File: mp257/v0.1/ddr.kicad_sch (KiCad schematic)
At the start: 61 parts, among them U1 STM32MP257FAK3, U15 MT40A1G16TB-062E IT:F

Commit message: Caps
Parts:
- added C158: 100nF_0402_16V, 4ms_Capacitor:C_0402, symbol 4ms_Capacitor:100nF_0402_16V
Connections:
- net GND: now also C158.2
- net VPP_DDR: now also C158.1
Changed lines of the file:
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@@
 	)
 	(junction
+		(at 208.28 243.84)
+		(diameter 0)
+		(color 0 0 0 0)
+	)
+	(junction
 		(at 241.3 123.19)
 		(diameter 0)
@@
 	(wire
 		(pts
+			(xy 198.12 251.46) (xy 208.28 251.46)
+		)
+		(stroke
+			(width 0)
+			(type default)
+		)
+	)
+	(wire
+		(pts
 			(xy 241.3 123.19) (xy 241.3 120.65)
 		)
@@
 	(wire
 		(pts
+			(xy 208.28 243.84) (xy 198.12 243.84)
+		)
+		(stroke
+			(width 0)
+			(type default)
+		)
+	)
+	(wire
+		(pts
 			(xy 241.3 135.89) (xy 241.3 143.51)
 		)
@@
 		)
 	)
+	(wire
+		(pts
+			(xy 198.12 243.84) (xy 198.12 246.38)
+		)
+		(stroke
+			(width 0)
+			(type default)
+		)
+	)
 	(label "DDR_A13"
 		(at 349.25 59.69 0)
@@
 					(unit 1)
 				)
+			)
+		)
+	)
+	(symbol
+		(lib_id "4ms_Capacitor:100nF_0402_16V")
+		(at 198.12 248.92 0)
+		(unit 1)
+		(exclude_from_sim no)
+		(in_bom yes)
+		(on_board yes)
+		(dnp no)
+		(fields_autoplaced yes)
+		(property "Reference" "C158"
+			(at 195.58 247.6562 0)
+			(effects
+				(font
+					(size 1.27 1.27)
+				)
+				(justify right)
+			)
+		)
+		(property "Value" "100nF_0402_16V"
+			(at 198.12 245.11 0)
+			(effects
+				(font
+					(size 1.27 1.27)
+				)
+				(hide yes)
+			)
+		)
+		(property "Footprint" "4ms_Capacitor:C_0402"
+			(at 195.58 254 0)
+			(effects
+				(font
+					(size 1.27 1.27)
+				)
+				(justify left)
+				(hide yes)
+			)
+		)
+		(property "Datasheet" ""
+			(at 198.12 248.92 0)
+			(effects
+				(font
+					(size 1.27 1.27)
+				)
+				(hide yes)
+			)
+		)
+		(property "Description" "0.1uF, Min. 16V 10%, X7R or X5R or similar"
+			(at 198.12 248.92 0)
+			(effects
+				(font
+					(size 1.27 1.27)
+				)
+				(hide yes)
+			)
+		)
+		(property "Specifications" "0.1uF, Min. 16V 10%, X7R or X5R or similar"
+			(at 195.58 256.794 0)
+			(effects
+				(font
+					(size 1.27 1.27)
+				)
+				(justify left)
+				(hide yes)
+			)
+		)
+		(property "Manufacturer" "Murata"
+			(at 195.58 258.318 0)
+			(effects
+				(font
+					(size 1.27 1.27)
+				)
+				(justify left)
+				(hide yes)
+			)
+		)
+		(property "Part Number" "GCM155R71C104KA55D"
+			(at 195.58 259.842 0)
+			(effects
+				(font
+					(size 1.27 1.27)
+				)
+				(justify left)
+				(hide yes)
+			)
+		)
+		(property "Display" "0.1uF"
+			(at 195.58 250.1962 0)
+			(effects
+				(font
+					(size 1.27 1.27)
+				)
+				(justify right)
+			)
+		)
+		(property "JLCPCB ID" "C1525"
+			(at 199.39 261.62 0)
+			(effects
+				(font
+					(size 1.27 1.27)
+				)
+				(hide yes)
+			)
+		)
+		(property "Manufacturer 2" "Yageo"
+			(at 199.39 262.89 0)
+			(effects
+				(font
+					(size 1.27 1.27)
+				)
+				(hide yes)
+			)
+		)
+		(property "Part Number 2" "CC0402KRX7R7BB104"
+			(at 205.74 265.43 0)
+			(effects
+				(font
+					(size 1.27 1.27)
+				)
+				(hide yes)
+			)
+		)
+		(property "Production Stage" "A"
+			(at 195.58 265.43 0)
+			(effects
+				(font
+					(size 1.27 1.27)
+				)
+				(justify left)
+				(hide yes)
+			)
+		)
+		(pin "1"
+		)
+		(pin "2"
+		)
+		(instances
+			(project "mp257-devboard"
+				(path "/64ec1a6b-f4f9-4414-abbd-a05816451f08/2d5e657e-c95b-4ad6-b4dc-8f322bebdc60"
+					(reference "C158")
+					(unit 1)
+				)

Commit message: Fix caps
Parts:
- added C211: 22uF_0603_6.3V, 4ms_Capacitor:C_0603, symbol 4ms_Capacitor:22uF_0603_6.3V
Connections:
- net GND: now also C211.2
- net VTT_DDR: now also C211.1
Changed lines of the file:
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@@
 	)
 	(junction
+		(at 377.19 57.15)
+		(diameter 0)
+		(color 0 0 0 0)
+	)
+	(junction
 		(at 307.34 109.22)
 		(diameter 0)
@@
 	(wire
 		(pts
+			(xy 377.19 57.15) (xy 389.89 57.15)
+		)
+		(stroke
+			(width 0)
+			(type default)
+		)
+	)
+	(wire
+		(pts
 			(xy 307.34 68.58) (xy 314.96 68.58)
 		)
@@
 	(wire
 		(pts
+			(xy 389.89 57.15) (xy 389.89 54.61)
+		)
+		(stroke
+			(width 0)
+			(type default)
+		)
+	)
+	(wire
+		(pts
 			(xy 369.57 130.81) (xy 377.19 130.81)
 		)
@@
 	(wire
 		(pts
+			(xy 377.19 49.53) (xy 389.89 49.53)
+		)
+		(stroke
+			(width 0)
+			(type default)
+		)
+	)
+	(wire
+		(pts
 			(xy 200.66 138.43) (xy 180.34 138.43)
 		)
@@
 					(unit 1)
 				)
+			)
+		)
+	)
+	(symbol
+		(lib_id "4ms_Capacitor:22uF_0603_6.3V")
+		(at 389.89 52.07 0)
+		(unit 1)
+		(exclude_from_sim no)
+		(in_bom yes)
+		(on_board yes)
+		(dnp no)
+		(property "Reference" "C211"
+			(at 390.906 49.022 0)
+			(effects
+				(font
+					(size 1.27 1.27)
+				)
+				(justify left bottom)
+			)
+		)
+		(property "Value" "22uF_0603_6.3V"
+			(at 389.89 48.26 0)
+			(effects
+				(font
+					(size 1.27 1.27)
+				)
+				(hide yes)
+			)
+		)
+		(property "Footprint" "4ms_Capacitor:C_0603"
+			(at 387.35 57.15 0)
+			(effects
+				(font
+					(size 1.27 1.27)
+				)
+				(justify left)
+				(hide yes)
+			)
+		)
+		(property "Datasheet" ""
+			(at 389.89 52.07 0)
+			(effects
+				(font
+					(size 1.27 1.27)
+				)
+				(hide yes)
+			)
+		)
+		(property "Description" "22uF, 6.3V,10%,X5R or X7R, 0603"
+			(at 389.89 52.07 0)
+			(effects
+				(font
+					(size 1.27 1.27)
+				)
+				(hide yes)
+			)
+		)
+		(property "Specifications" "22uF, 6.3V,10%,X5R or X7R,0603"
+			(at 387.35 59.944 0)
+			(effects
+				(font
+					(size 1.27 1.27)
+				)
+				(justify left)
+				(hide yes)
+			)
+		)
+		(property "Manufacturer" "Murata"
+			(at 387.35 61.468 0)
+			(effects
+				(font
+					(size 1.27 1.27)
+				)
+				(justify left)
+				(hide yes)
+			)
+		)
+		(property "Part Number" "GRM188R60J226MEA0J"
+			(at 387.35 62.992 0)
+			(effects
+				(font
+					(size 1.27 1.27)
+				)
+				(justify left)
+				(hide yes)
+			)
+		)
+		(property "Display" "22uF/6.3V"
+			(at 392.43 45.974 0)
+			(effects
+				(font
+					(size 1.27 1.27)
+				)
+				(justify left)
+			)
+		)
+		(property "JLCPCB ID" "C59461"
+			(at 389.89 52.07 0)
+			(effects
+				(font
+					(size 1.27 1.27)
+				)
+				(hide yes)
+			)
+		)
+		(property "Production Stage" "A"
+			(at 387.35 68.58 0)
+			(effects
+				(font
+					(size 1.27 1.27)
+				)
+				(justify left)
+				(hide yes)
+			)
+		)
+		(pin "1"
+		)
+		(pin "2"
+		)
+		(instances
+			(project "mp257-devboard"
+				(path "/64ec1a6b-f4f9-4414-abbd-a05816451f08/2d5e657e-c95b-4ad6-b4dc-8f322bebdc60"
+					(reference "C211")
+					(unit 1)
+				)

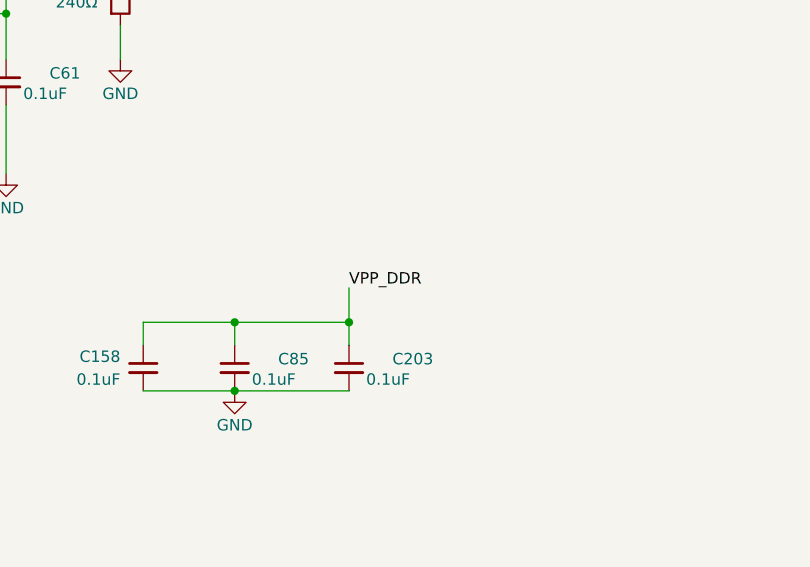
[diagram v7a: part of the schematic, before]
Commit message: pmic placement
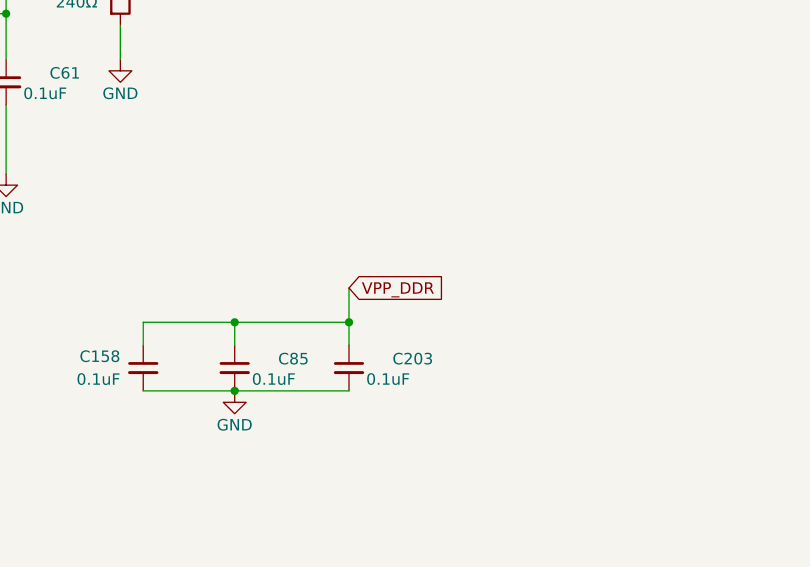
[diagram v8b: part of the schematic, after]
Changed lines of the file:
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@@
-		)
-	)
-	(label "VPP_DDR"
-		(at 220.98 240.03 0)
-		(effects
-			(font
-				(size 1.27 1.27)
-			)
-			(justify left bottom)
 		)
 	)
@@
 		)
 	)
+	(global_label "VPP_DDR"
+		(shape input)
+		(at 220.98 240.03 0)
+		(fields_autoplaced yes)
+		(effects
+			(font
+				(size 1.27 1.27)
+			)
+			(justify left)
+		)
+		(property "Intersheetrefs" "${INTERSHEET_REFS}"
+			(at 232.3714 240.03 0)
+			(effects
+				(font
+					(size 1.27 1.27)
+				)
+				(justify left)
+				(hide yes)
+			)
+		)
+	)
